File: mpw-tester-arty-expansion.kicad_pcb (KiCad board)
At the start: 4 copper layers, 53.3 x 61.5 mm, 132 parts, among them J1 USB4105-GF-A, J10 61300211121, J11 61300211121, J12 61300211121, J14 61300311121, J15 61300311121, J18 61300411121, J19 61300711121, J2 61300211121, J20 61300411121, J3 Arty_A7_SPI, J4 61300211121, J5 61300311121, J6 61300211121, J7 61300211121, J8 61300211121, J9 61300211121, Q1 DTC014TEBTL, SW1 JS202011JCQN, U1 SN74LVC1G125DCKR, U2 FT232HQ, U3 SN74LVC1G125DCKR, U4 MAX811REUS+T, U5 NTS0102DP, U6 MCP4661-103E/ML, U7 Caravel_breakout_PCB, U8 W25Q32FVSS, U9 MIC2211-AAYML-TR, Y1 ABM8G-12.000MHZ-18-D2Y-T, Y2 ECS-2520MVLC-100-BN-TR

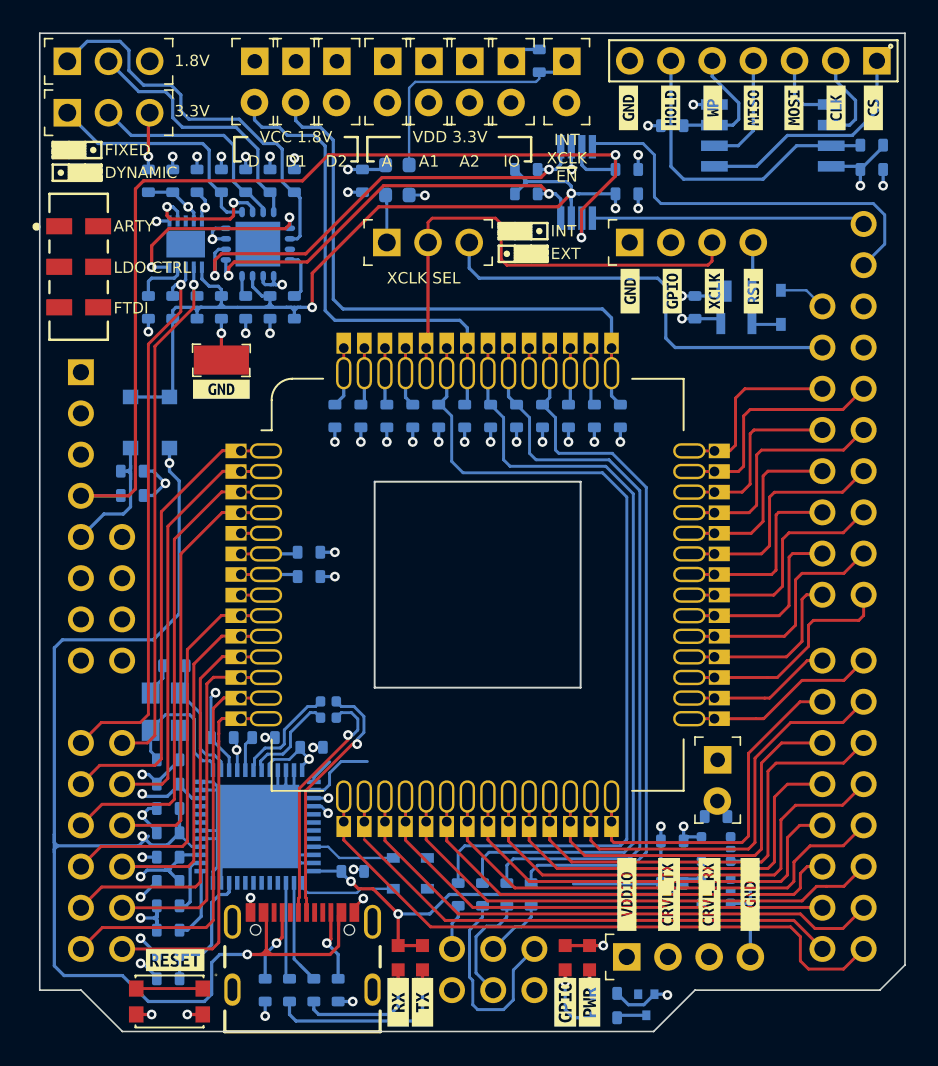
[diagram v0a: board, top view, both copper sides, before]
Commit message: Update FT232H footprint
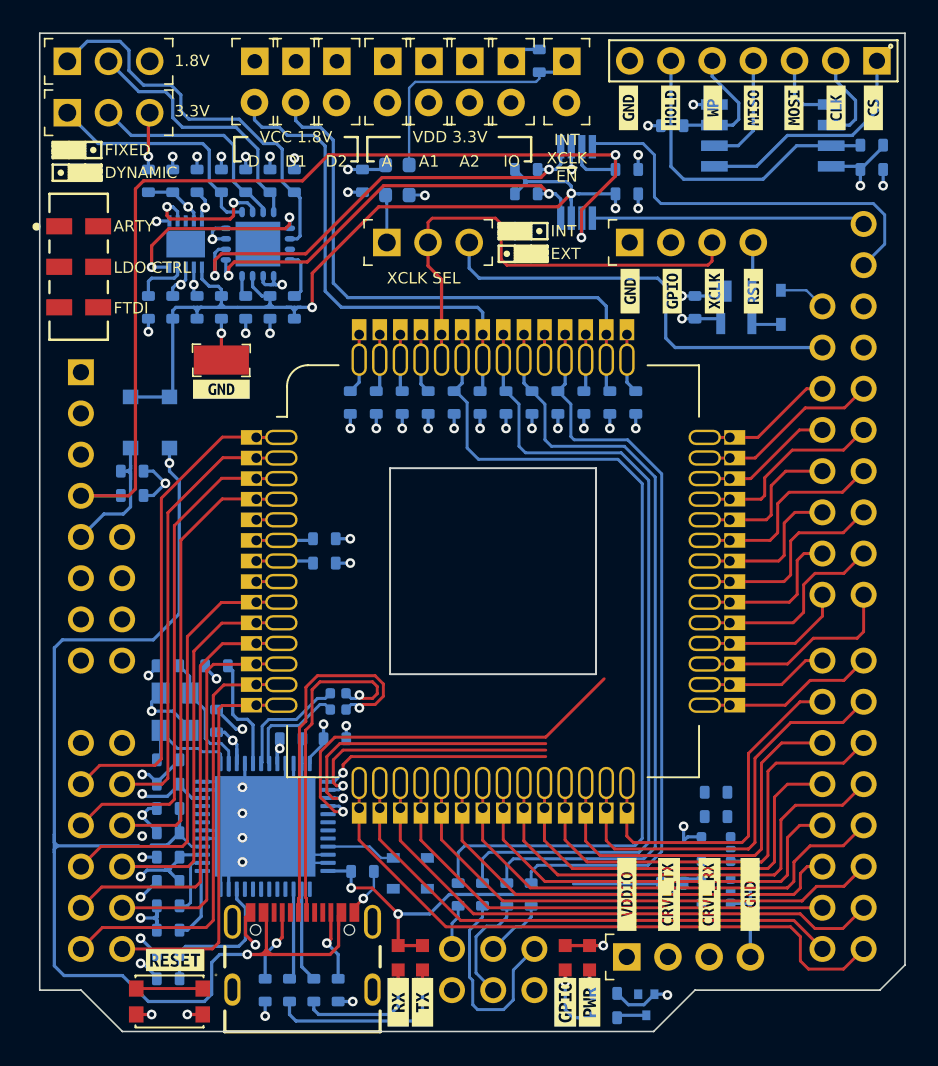
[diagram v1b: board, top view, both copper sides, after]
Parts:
- removed J2: 61300211121, antmicro-footprints:PinHeader_1x2_P2.54_Drill0.9mm
- added C13: C_100n_0603, antmicro-footprints:0603-cap, B.Cu at (141.2, 109.5)
- U2: footprint antmicro-footprints:QFN-48-1EP_7x7mm -> antmicro-footprints:QFN-48-1EP_8x8mm_P0.5mm_EP6.2x6.2mm_FT232HQ_marking
- moved R7 5.29 mm to (133.9, 105.0), turned to 0 degrees
- moved C10 4.04 mm to (164.7, 112.8)
- moved C8 1.37 mm to (138.5, 109.5)
- moved C22 1.26 mm to (142.2, 88.8)
- moved C26 1.26 mm to (140.6, 98.7)
- moved C27 1.26 mm to (158.2, 88.8)
- moved C28 1.26 mm to (140.6, 97.2)
- moved C30 1.26 mm to (156.6, 88.8)
- moved C31 1.26 mm to (150.2, 88.8)
- moved R17 1.26 mm to (148.6, 88.8)
- moved C23 1.26 mm to (145.3, 88.8)
- moved C24 1.26 mm to (159.8, 88.8)
- moved C29 1.26 mm to (143.8, 88.8)
- moved R18 1.26 mm to (154.9, 88.8)
- moved R19 1.26 mm to (151.8, 88.8)
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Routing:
- net /VCCD1: track 36.9 -> 3.72 mm
- net /EN_VOUT2: track 34.5 -> 2.28 mm
- net /EN_VOUT1: track 32.9 -> 1.86 mm
- net AGND: track 117.3 -> 142.7 mm, vias 47 -> 51
- net /CRVL_IO3: track 15.7 -> 37.3 mm
- net /MEM.SCK: track 49.9 -> 69.9 mm
- net /CRVL_IO1: track 15.6 -> 29.7 mm
- net /CRVL_IO4: track 13.1 -> 23.9 mm, vias 0 -> 1
- net /CRVL_IO2: track 16.1 -> 25.0 mm, vias 0 -> 1
- net /VDDA1: track 27.3 -> 35.5 mm
- net /USB_DP: track 15.7 -> 23.4 mm
- net /FTDI_~{MR}: track 6.13 -> 0.00 mm
- net /USB_DN: track 16.4 -> 21.6 mm
- net /REF: track 2.11 -> 7.02 mm
- net /VDDA: track 21.8 -> 26.0 mm
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
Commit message: Swap Arty_EN_VOUT 1 and 2. Continue layout
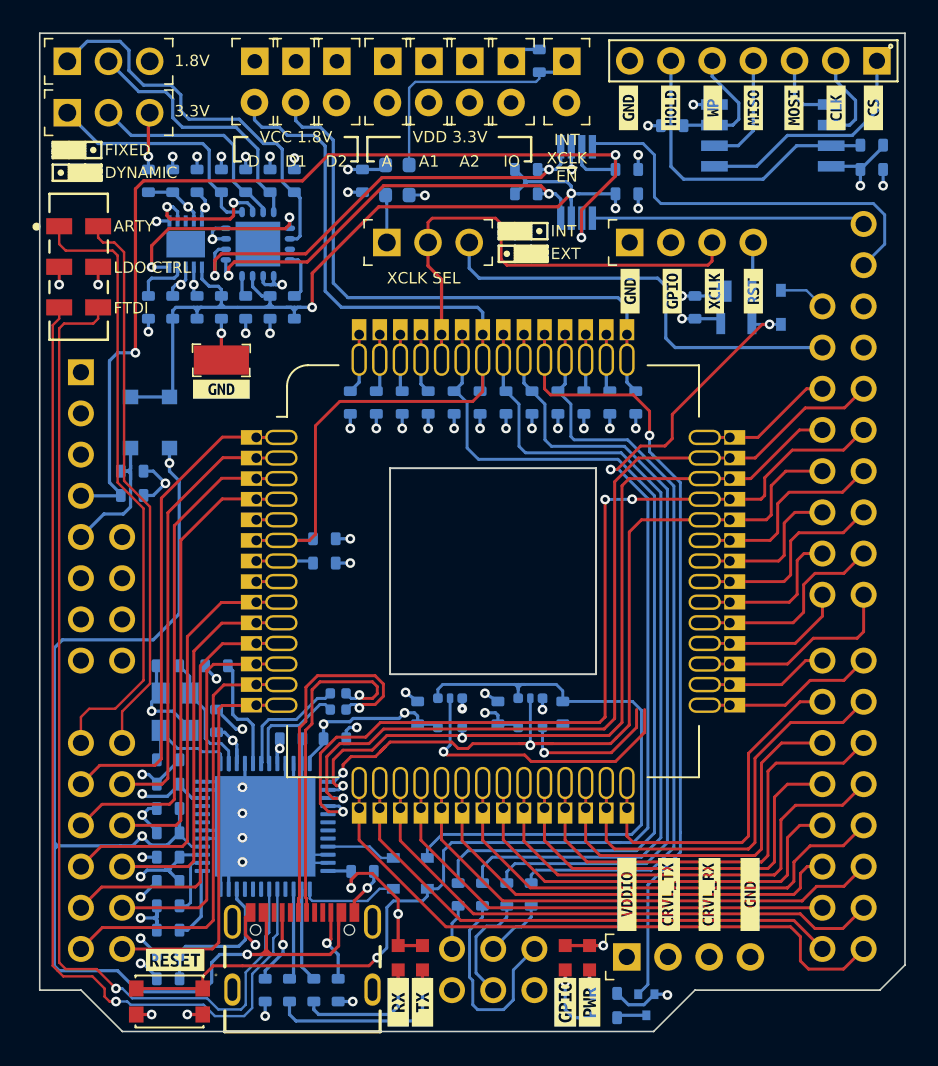
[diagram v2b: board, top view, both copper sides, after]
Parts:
- moved U3 19.7 mm to (148.3, 107.9), turned to 0 degrees
- moved C18 18.9 mm to (146.3, 107.9), turned to 90 degrees
- moved C10 14.3 mm to (151.2, 107.9), turned to 90 degrees
- moved U1 14.2 mm to (153.2, 107.9), turned to 0 degrees
- moved R1 11.4 mm to (155.2, 107.9), turned to -90 degrees
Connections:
- J3 pad 19: /ARTY_EN_VOUT1 -> /ARTY_EN_VOUT2
- J3 pad 9: /ARTY_EN_VOUT2 -> /ARTY_EN_VOUT1
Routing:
- net /~{MR}: track 5.91 -> 79.0 mm, vias 0 -> 3
- net /FTDI_EN_VOUT2: track 0.00 -> 63.0 mm, vias 0 -> 1
- net /FTDI_EN_VOUT1: track 0.00 -> 62.8 mm, vias 0 -> 1
- net /CRVL_GPIO: track 1.55 -> 48.2 mm, vias 0 -> 1
- net /ARTY_EN_VOUT1: track 0.00 -> 38.2 mm
- net /~{UART_EN}: track 0.00 -> 37.4 mm
- net /ARTY_EN_VOUT2: track 0.00 -> 34.3 mm
- net /VCCD1: track 3.72 -> 36.9 mm
- net /CRVL_IO4: track 23.9 -> 52.5 mm, vias 1 -> 2
- net /CRVL_IO2: track 25.0 -> 51.0 mm, vias 1 -> 2
- net /CRVL_IO1: track 29.7 -> 55.4 mm
- net /VCCD: track 33.8 -> 55.9 mm
- net /CRVL_IO3: track 37.3 -> 56.1 mm, vias 1 -> 3
- net /CRVL_IO6: track 9.67 -> 27.9 mm, vias 0 -> 1
- net /MEM.SCK: track 69.9 -> 52.5 mm
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
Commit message: Finish routing of the board without UART_EN header
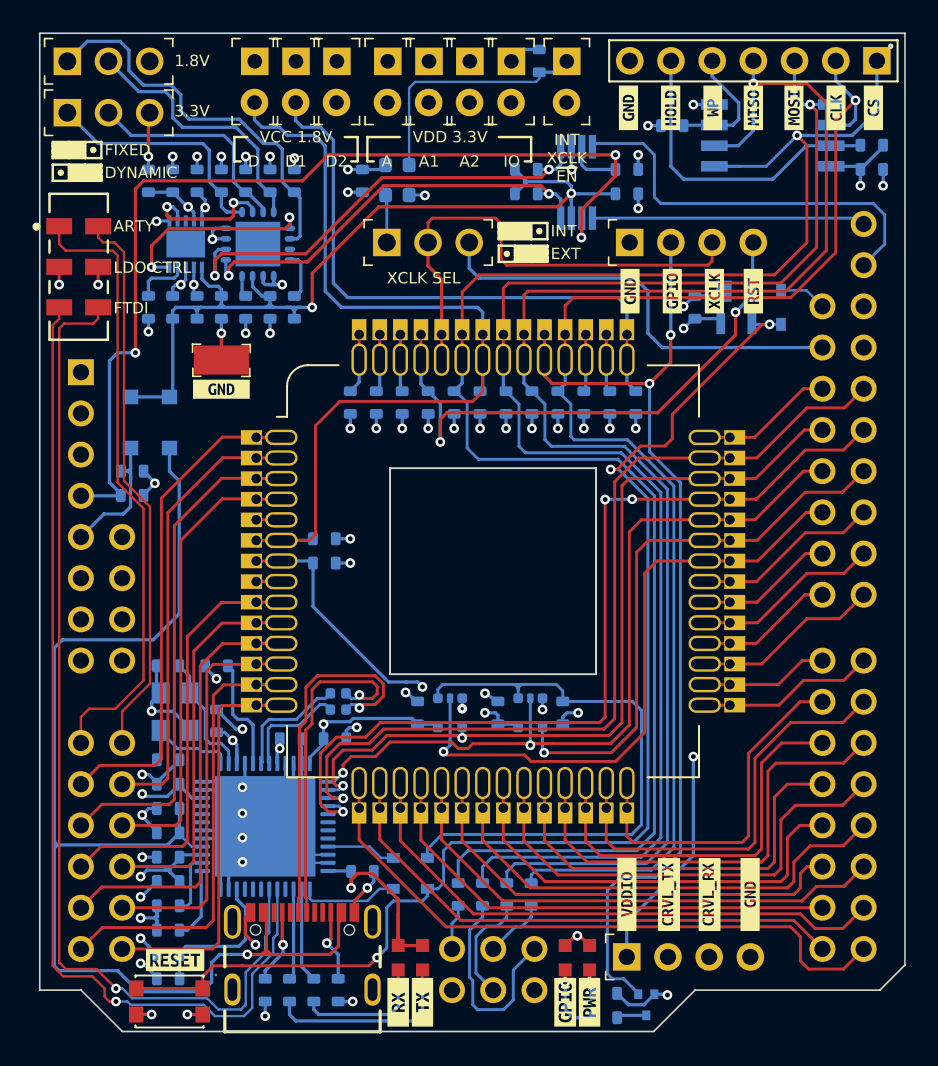
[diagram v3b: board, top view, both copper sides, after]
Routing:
- net /VDDIO: track 39.9 -> 84.0 mm, vias 0 -> 2
- net /CRVL_IO6: track 27.9 -> 67.4 mm
- net /MEM.SO: track 56.1 -> 92.4 mm, vias 0 -> 1
- net /CRVL_IO5: track 21.7 -> 55.4 mm
- net /MEM.SI: track 55.9 -> 88.1 mm, vias 0 -> 1
- net /MEM.~{CS}: track 69.9 -> 101.9 mm, vias 0 -> 1
- net /MEM.SCK: track 52.5 -> 82.2 mm, vias 0 -> 1
- net /CRVL_~{RST}: track 6.19 -> 34.5 mm, vias 0 -> 2
- net /CRVL_GPIO: track 48.2 -> 61.2 mm, vias 1 -> 2
- net AGND: track 133.7 -> 131.4 mm
- net /FTDI_3V3: track 41.3 -> 43.5 mm, vias 9 -> 7
- net VBUS: track 77.6 -> 76.1 mm, vias 3 -> 1
- net /CRVL_IO4: track 52.5 -> 51.0 mm
- net /CRVL_IO11: track 12.9 -> 11.6 mm
- net /CRVL_IO8: track 9.73 -> 8.50 mm
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
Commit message: Add slide switches for Arty powered from USB and UART buffer ctrl
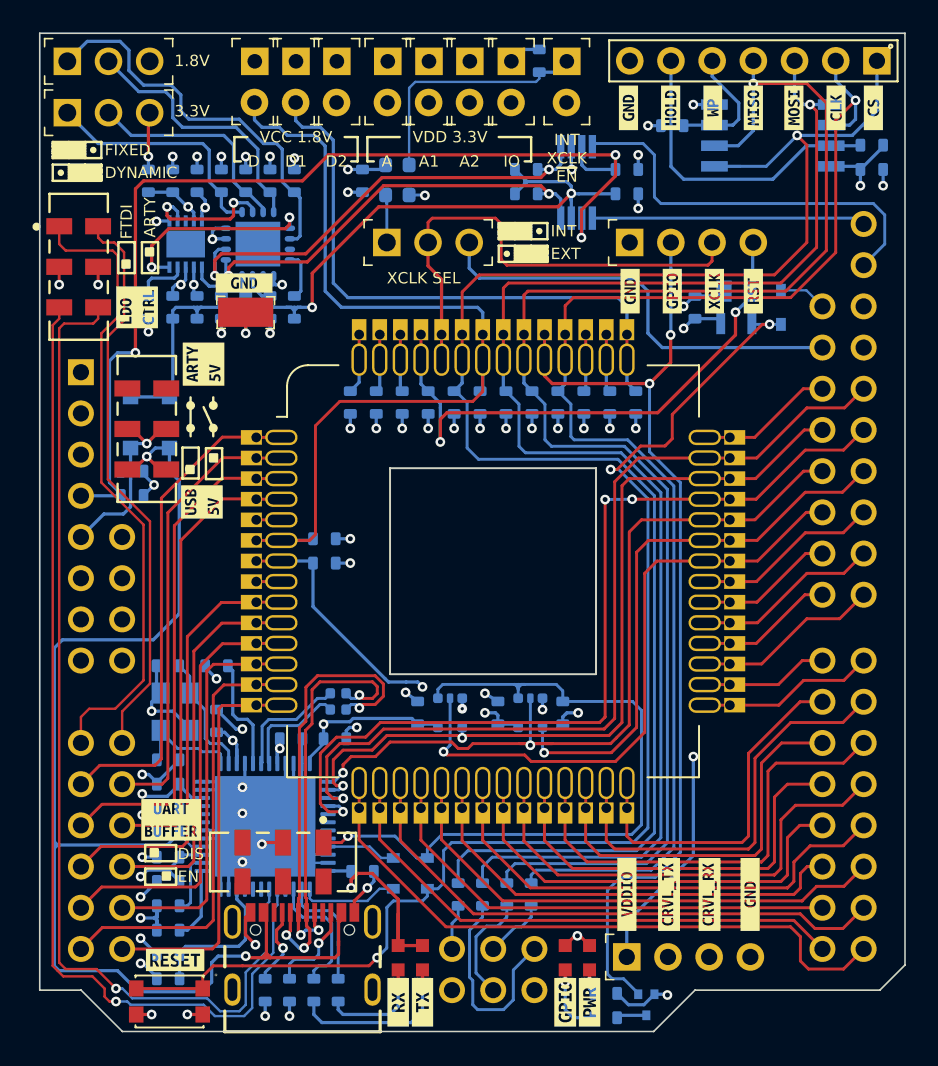
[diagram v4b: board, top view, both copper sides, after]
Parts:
- added SW2: JS202011JCQN, antmicro-footprints:JS202011JCQN, F.Cu at (138.0, 117.1)
- added SW3: JS202011JCQN, antmicro-footprints:JS202011JCQN, F.Cu at (129.6, 90.4)
- added kibuzzard-63938A8C: G***, kibuzzard-63938A8C, F.Cu at (129.0, 82.9)
- added kibuzzard-63938B4C: G***, kibuzzard-63938B4C, F.Cu at (131.1, 114.5)
- added kibuzzard-6393906F: G***, kibuzzard-6393906F, F.Cu at (133.1, 86.4)
- added kibuzzard-639390A2: G***, kibuzzard-639390A2, F.Cu at (133.0, 94.9)
- moved kibuzzard-638FA1CB 6.70 mm to (135.6, 81.4)
- moved TP1 3.31 mm to (135.7, 83.2)
- moved R3 3.00 mm to (138.4, 125.0)
- moved R10 1.50 mm to (139.9, 125.0)
- moved R9 1.50 mm to (141.4, 125.0)
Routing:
- net /~{UART_EN}: track 37.4 -> 44.5 mm, vias 0 -> 1
- net VBUS: track 76.1 -> 81.8 mm, vias 1 -> 2
- net /USB_DN: track 21.6 -> 26.9 mm, vias 1 -> 3
- net /5V0_ARTY: track 9.10 -> 13.4 mm, vias 0 -> 1
- net /USB_DP: track 23.4 -> 27.3 mm, vias 1 -> 3
- net /~{TX_LED}: track 5.63 -> 8.07 mm
- net Net-(D1-Pad2): track 8.28 -> 6.78 mm
- net Net-(D2-Pad2): track 12.0 -> 10.5 mm
- net /~{RX_LED}: track 5.84 -> 7.28 mm
- net /CC2: track 4.48 -> 5.85 mm
- net AGND: track 131.4 -> 132.4 mm
- net /ARTY_EN_VOUT1: track 38.2 -> 39.1 mm
- net /ARTY_EN_VOUT2: track 34.3 -> 35.1 mm
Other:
- board text added: "DIS"
- board text added: "EN"
- board text removed: "LDO CTRL"

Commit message: Add USB TVS, finish layout, resolve DRC
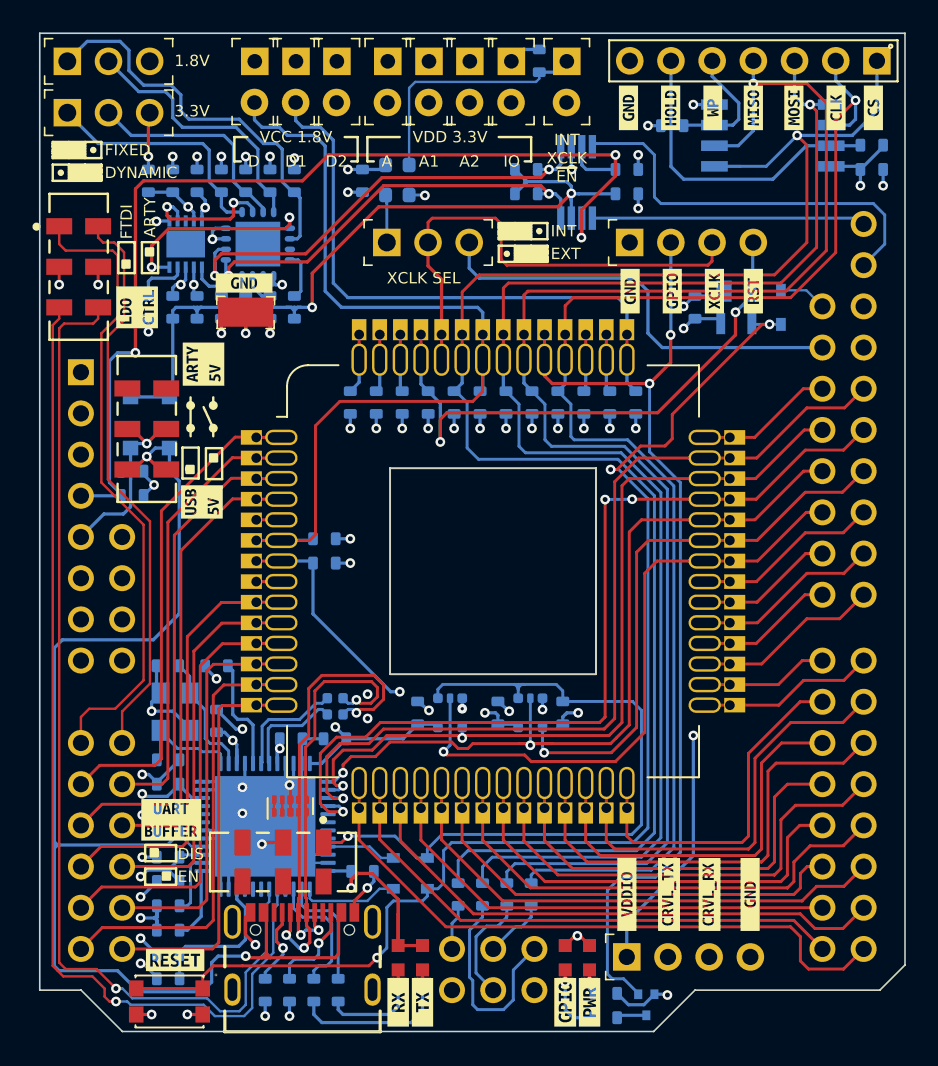
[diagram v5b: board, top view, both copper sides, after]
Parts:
- added U10: TPD4E02B04DQA, antmicro-footprints:USON-10_2.5x1.0mm_P0.5mm, F.Cu at (138.4, 113.7)
- moved R4 0.35 mm to (141.2, 107.0)
- moved R5 0.35 mm to (141.2, 108.0)
- turned C13 to 180 degrees
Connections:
- J1 pad S1: unconnected-(J1-PadS1) -> AGND
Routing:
- net AGND: track 132.4 -> 135.7 mm, vias 54 -> 55
- net /VDDIO: track 84.0 -> 84.9 mm
- net unconnected-(U10-Pad2): track 0.00 -> 0.77 mm
- net unconnected-(U10-Pad1): track 0.00 -> 0.77 mm
- net VBUS: track 81.8 -> 81.2 mm

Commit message: Loclib
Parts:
- C1, C10, C11, C12, C13, C14, C15, C16, C17, C18, C19, C2, C20, C21, C22, C23, C24, C25, C26, C27, C28, C29, C3, C30, C31, C32, C33, C34, C35, C36, C37, C4, C5, C6, C7, C8, C9: footprint antmicro-footprints:0603-cap -> mpw-tester-arty-expansion-footprints:0603-cap
- D1, D2, D3, D4: footprint antmicro-footprints:LED_0603 -> mpw-tester-arty-expansion-footprints:LED_0603
- D5, D6, D9: footprint antmicro-footprints:SOD-323F -> mpw-tester-arty-expansion-footprints:SOD-323F
- D7, D8: footprint antmicro-footprints:SOD-123 -> mpw-tester-arty-expansion-footprints:SOD-123
- J1: footprint antmicro-footprints:GCT_USB4105-GF-A -> mpw-tester-arty-expansion-footprints:GCT_USB4105-GF-A
- J10, J11, J12, J4, J6, J7, J8, J9: footprint antmicro-footprints:PinHeader_1x2_P2.54_Drill0.9mm -> mpw-tester-arty-expansion-footprints:PinHeader_1x2_P2.54_Drill0.9mm
- J14, J15, J5: footprint antmicro-footprints:PinHeader_1x3_P2.54_Drill1.1mm -> mpw-tester-arty-expansion-footprints:PinHeader_1x3_P2.54_Drill1.1mm
- J18, J20: footprint antmicro-footprints:PinHeader_1x4_P2.54mm_Drill1.02mm -> mpw-tester-arty-expansion-footprints:PinHeader_1x4_P2.54mm_Drill1.02mm
- J19: footprint antmicro-footprints:61300711121 -> mpw-tester-arty-expansion-footprints:61300711121
- J3: footprint antmicro-footprints:ARTY_A7_SHIELD -> mpw-tester-arty-expansion-footprints:ARTY_A7_SHIELD
- Q1: footprint antmicro-footprints:SOT-416 -> mpw-tester-arty-expansion-footprints:SOT-416
- R1, R10, R11, R12, R13, R14, R15, R16, R17, R18, R19, R2, R20, R21, R22, R23, R24, R25, R26, R27, R28, R29, R3, R30, R31, R32, R33, R34, R6, R7, R8, R9: footprint antmicro-footprints:0603-res -> mpw-tester-arty-expansion-footprints:0603-res
- R4, R5: footprint antmicro-footprints:0402-res -> mpw-tester-arty-expansion-footprints:0402-res
- S1: footprint antmicro-footprints:SW_SPST_4.2x2.8 -> mpw-tester-arty-expansion-footprints:SW_SPST_4.2x2.8
- SW1, SW2, SW3: footprint antmicro-footprints:JS202011JCQN -> mpw-tester-arty-expansion-footprints:JS202011JCQN
- TP1: footprint antmicro-footprints:PROBE_PAD_1206 -> mpw-tester-arty-expansion-footprints:PROBE_PAD_1206
- U1, U3: footprint antmicro-footprints:SOT-353 -> mpw-tester-arty-expansion-footprints:SOT-353
- U10: footprint antmicro-footprints:USON-10_2.5x1.0mm_P0.5mm -> mpw-tester-arty-expansion-footprints:USON-10_2.5x1.0mm_P0.5mm
- U2: footprint antmicro-footprints:QFN-48-1EP_8x8mm_P0.5mm_EP6.2x6.2mm_FT232HQ_marking -> mpw-tester-arty-expansion-footprints:QFN-48-1EP_8x8mm_P0.5mm_EP6.2x6.2mm_FT232HQ_marking
- U4: footprint antmicro-footprints:SOT-143-4 -> mpw-tester-arty-expansion-footprints:SOT-143-4
- U5: footprint antmicro-footprints:TSSOP-8_W3mm -> mpw-tester-arty-expansion-footprints:TSSOP-8_W3mm
- U6: footprint antmicro-footprints:QFN-16_EP_4x4_Pitch0.65mm -> mpw-tester-arty-expansion-footprints:QFN-16_EP_4x4_Pitch0.65mm
- U7: footprint antmicro-footprints:caravel_breakout -> mpw-tester-arty-expansion-footprints:caravel_breakout
- U8: footprint antmicro-footprints:SOIC127P790X216-8N -> mpw-tester-arty-expansion-footprints:SOIC127P790X216-8N
- U9: footprint antmicro-footprints:DFN-10-1EP_3x3mm -> mpw-tester-arty-expansion-footprints:DFN-10-1EP_3x3mm
- Y1: footprint antmicro-footprints:KX-7 -> mpw-tester-arty-expansion-footprints:KX-7
- Y2: footprint antmicro-footprints:Oscillator_SMD_ECS_2520MV-xxx-xx-4Pin_2.5x2.0mm -> mpw-tester-arty-expansion-footprints:Oscillator_SMD_ECS_2520MV-xxx-xx-4Pin_2.5x2.0mm
